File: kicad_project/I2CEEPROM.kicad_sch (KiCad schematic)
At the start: 3 parts, among them U15 24FC64-I/SN

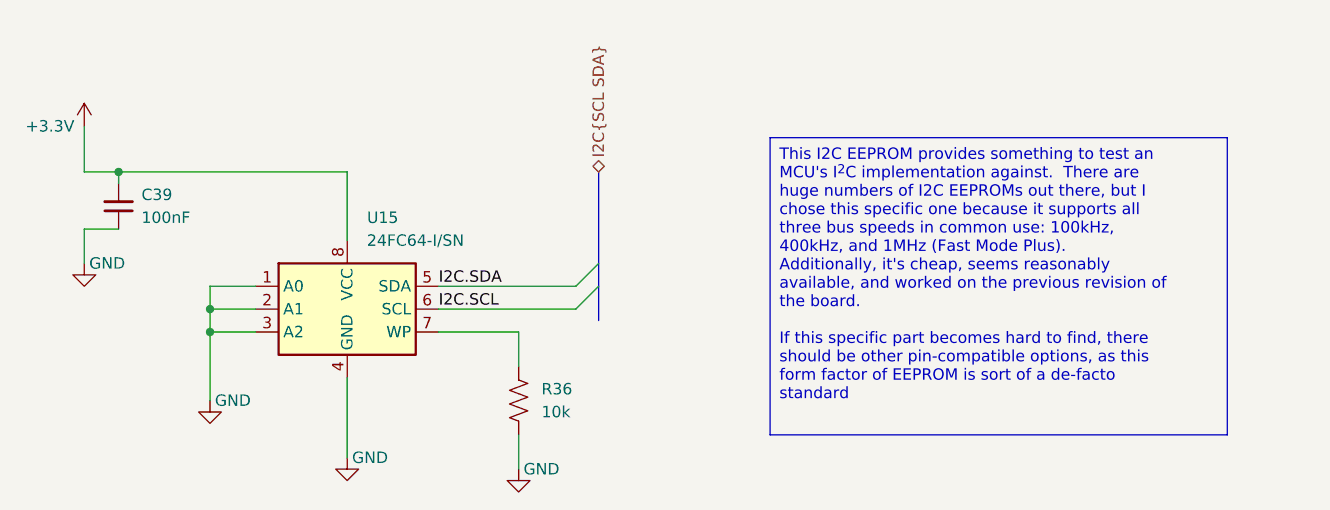
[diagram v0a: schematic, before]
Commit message: Switch out multiplexer, start switch FX2LP out for RP2040
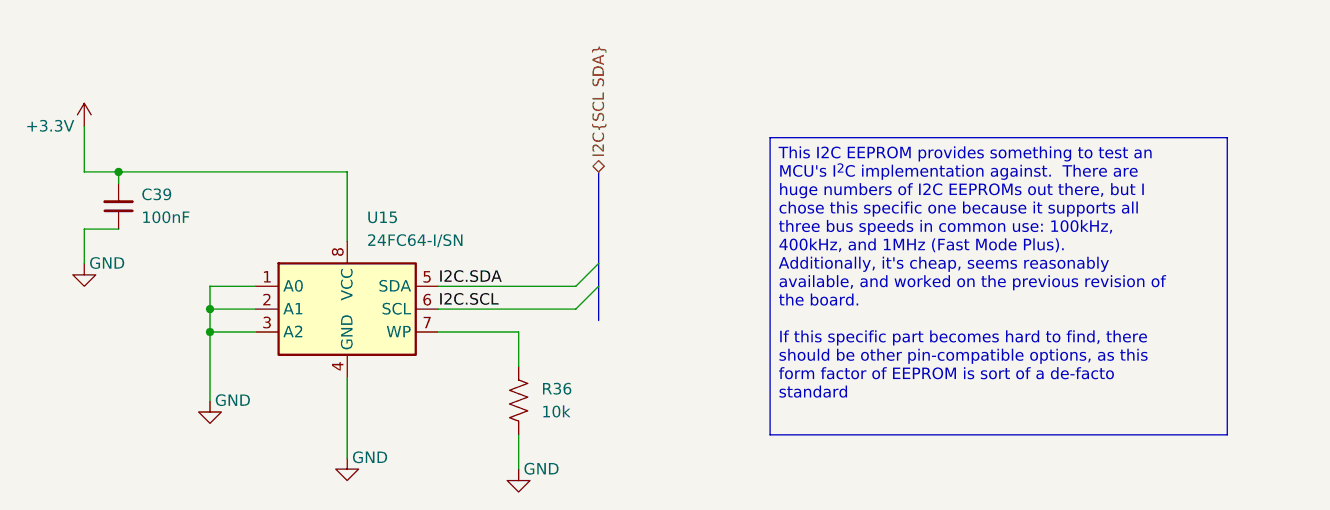
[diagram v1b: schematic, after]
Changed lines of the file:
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@@
 (kicad_sch
-	(version 20231120)
+	(version 20250114)
 	(generator "eeschema")
-	(generator_version "8.0")
+	(generator_version "9.0")
 	(paper "A5")
 	(title_block
@@
 		(comment 1 "EEPROM for the board to talk to over I^{2}C")
 	)
-	(junction
-		(at 67.31 53.34)
-		(diameter 0)
-		(color 0 0 0 0)
-	)
-	(junction
-		(at 77.47 68.58)
-		(diameter 0)
-		(color 0 0 0 0)
-	)
-	(junction
-		(at 77.47 71.12)
-		(diameter 0)
-		(color 0 0 0 0)
-	)
-	(bus_entry
-		(at 120.65 63.5)
-		(size -2.54 2.54)
-		(stroke
-			(width 0)
-			(type default)
-		)
-	)
-	(bus_entry
-		(at 120.65 66.04)
-		(size -2.54 2.54)
-		(stroke
-			(width 0)
-			(type default)
-		)
-	)
-	(wire
-		(pts
-			(xy 77.47 71.12) (xy 77.47 78.74)
-		)
-		(stroke
-			(width 0)
-			(type default)
-		)
-	)
-	(wire
-		(pts
-			(xy 77.47 68.58) (xy 77.47 71.12)
-		)
-		(stroke
-			(width 0)
-			(type default)
-		)
-	)
-	(wire
-		(pts
-			(xy 63.5 53.34) (xy 67.31 53.34)
-		)
-		(stroke
-			(width 0)
-			(type default)
-		)
-	)
-	(wire
-		(pts
-			(xy 67.31 53.34) (xy 67.31 54.61)
-		)
-		(stroke
-			(width 0)
-			(type default)
-		)
-	)
-	(wire
-		(pts
-			(xy 67.31 53.34) (xy 92.71 53.34)
-		)
-		(stroke
-			(width 0)
-			(type default)
-		)
-	)
-	(bus
-		(pts
-			(xy 120.65 53.34) (xy 120.65 63.5)
-		)
-		(stroke
-			(width 0)
-			(type default)
-		)
-	)
-	(wire
-		(pts
-			(xy 92.71 76.2) (xy 92.71 85.09)
-		)
-		(stroke
-			(width 0)
-			(type default)
-		)
-	)
-	(wire
-		(pts
-			(xy 82.55 68.58) (xy 77.47 68.58)
-		)
-		(stroke
-			(width 0)
-			(type default)
-		)
-	)
-	(wire
-		(pts
-			(xy 111.76 71.12) (xy 111.76 74.93)
-		)
-		(stroke
-			(width 0)
-			(type default)
-		)
-	)
-	(bus
-		(pts
-			(xy 120.65 63.5) (xy 120.65 66.04)
-		)
-		(stroke
-			(width 0)
-			(type default)
-		)
-	)
-	(wire
-		(pts
-			(xy 77.47 66.04) (xy 77.47 68.58)
-		)
-		(stroke
-			(width 0)
-			(type default)
-		)
-	)
-	(wire
-		(pts
-			(xy 67.31 59.69) (xy 63.5 59.69)
-		)
-		(stroke
-			(width 0)
-			(type default)
-		)
-	)
-	(wire
-		(pts
-			(xy 111.76 82.55) (xy 111.76 86.36)
-		)
-		(stroke
-			(width 0)
-			(type default)
-		)
-	)
-	(wire
-		(pts
-			(xy 63.5 59.69) (xy 63.5 63.5)
-		)
-		(stroke
-			(width 0)
-			(type default)
-		)
-	)
-	(wire
-		(pts
-			(xy 63.5 48.26) (xy 63.5 53.34)
-		)
-		(stroke
-			(width 0)
-			(type default)
-		)
-	)
-	(wire
-		(pts
-			(xy 102.87 71.12) (xy 111.76 71.12)
-		)
-		(stroke
-			(width 0)
-			(type default)
-		)
-	)
-	(wire
-		(pts
-			(xy 92.71 53.34) (xy 92.71 60.96)
-		)
-		(stroke
-			(width 0)
-			(type default)
-		)
-	)
-	(wire
-		(pts
-			(xy 82.55 66.04) (xy 77.47 66.04)
-		)
-		(stroke
-			(width 0)
-			(type default)
-		)
-	)
-	(wire
-		(pts
-			(xy 102.87 66.04) (xy 118.11 66.04)
-		)
-		(stroke
-			(width 0)
-			(type default)
-		)
-	)
-	(wire
-		(pts
-			(xy 82.55 71.12) (xy 77.47 71.12)
-		)
-		(stroke
-			(width 0)
-			(type default)
-		)
-	)
-	(wire
-		(pts
-			(xy 102.87 68.58) (xy 118.11 68.58)
-		)
-		(stroke
-			(width 0)
-			(type default)
-		)
-	)
-	(bus
-		(pts
-			(xy 120.65 66.04) (xy 120.65 69.85)
-		)
-		(stroke
-			(width 0)
-			(type default)
-		)
-	)
 	(text_box "This I2C EEPROM provides something to test an MCU's I^{2}C implementation against.  There are huge numbers of I2C EEPROMs out there, but I chose this specific one because it supports all three bus speeds in common use: 100kHz, 400kHz, and 1MHz (Fast Mode Plus).  Additionally, it's cheap, seems reasonably available, and worked on the previous revision of the board.\n\nIf this specific part becomes hard to find, there should be other pin-compatible options, as this form factor of EEPROM is sort of a de-facto standard"
 		(exclude_from_sim no)
 		(at 139.7 49.53 0)
 		(size 50.8 33.02)
+		(margins 0.9525 0.9525 0.9525 0.9525)
 		(stroke
 			(width 0)
@@
 		)
 	)
+	(junction
+		(at 67.31 53.34)
+		(diameter 0)
+		(color 0 0 0 0)
+	)
+	(junction
+		(at 77.47 68.58)
+		(diameter 0)
+		(color 0 0 0 0)
+	)
+	(junction
+		(at 77.47 71.12)
+		(diameter 0)
+		(color 0 0 0 0)
+	)
+	(bus_entry
+		(at 120.65 63.5)
+		(size -2.54 2.54)
+		(stroke
+			(width 0)
+			(type default)
+		)
+	)
+	(bus_entry
+		(at 120.65 66.04)
+		(size -2.54 2.54)
+		(stroke
+			(width 0)
+			(type default)
+		)
+	)
+	(wire
+		(pts
+			(xy 77.47 71.12) (xy 77.47 78.74)
+		)
+		(stroke
+			(width 0)
+			(type default)
+		)
+	)
+	(wire
+		(pts
+			(xy 77.47 68.58) (xy 77.47 71.12)
+		)
+		(stroke
+			(width 0)
+			(type default)
+		)
+	)
+	(wire
+		(pts
+			(xy 63.5 53.34) (xy 67.31 53.34)
+		)
+		(stroke
+			(width 0)
+			(type default)
+		)
+	)
+	(wire
+		(pts
+			(xy 67.31 53.34) (xy 67.31 54.61)
+		)
+		(stroke
+			(width 0)
+			(type default)
+		)
+	)
+	(wire
+		(pts
+			(xy 67.31 53.34) (xy 92.71 53.34)
+		)
+		(stroke
+			(width 0)
+			(type default)
+		)
+	)
+	(bus
+		(pts
+			(xy 120.65 53.34) (xy 120.65 63.5)
+		)
+		(stroke
+			(width 0)
+			(type default)
+		)
+	)
+	(wire
+		(pts
+			(xy 92.71 76.2) (xy 92.71 85.09)
+		)
+		(stroke
+			(width 0)
+			(type default)
+		)
+	)
+	(wire
+		(pts
+			(xy 82.55 68.58) (xy 77.47 68.58)
+		)
+		(stroke
+			(width 0)
+			(type default)
+		)
+	)
+	(wire
+		(pts
+			(xy 111.76 71.12) (xy 111.76 74.93)
+		)
+		(stroke
+			(width 0)
+			(type default)
+		)
+	)
+	(bus
+		(pts
+			(xy 120.65 63.5) (xy 120.65 66.04)
+		)
+		(stroke
+			(width 0)
+			(type default)
+		)
+	)
+	(wire
+		(pts
+			(xy 77.47 66.04) (xy 77.47 68.58)
+		)
+		(stroke
+			(width 0)
+			(type default)
+		)
+	)
+	(wire
+		(pts
+			(xy 67.31 59.69) (xy 63.5 59.69)
+		)
+		(stroke
+			(width 0)
+			(type default)
+		)
+	)
+	(wire
+		(pts
+			(xy 111.76 82.55) (xy 111.76 86.36)
+		)
+		(stroke
+			(width 0)
+			(type default)
+		)
+	)
+	(wire
+		(pts
+			(xy 63.5 59.69) (xy 63.5 63.5)
+		)
+		(stroke
+			(width 0)
+			(type default)
+		)
+	)
+	(wire
+		(pts
+			(xy 63.5 48.26) (xy 63.5 53.34)
+		)
+		(stroke
+			(width 0)
+			(type default)
+		)
+	)
+	(wire
+		(pts
+			(xy 102.87 71.12) (xy 111.76 71.12)
+		)
+		(stroke
+			(width 0)
+			(type default)
+		)
+	)
+	(wire
+		(pts
+			(xy 92.71 53.34) (xy 92.71 60.96)
+		)
+		(stroke
+			(width 0)
+			(type default)
+		)
+	)
+	(wire
+		(pts
+			(xy 82.55 66.04) (xy 77.47 66.04)
+		)
+		(stroke
+			(width 0)
+			(type default)
+		)
+	)
+	(wire
+		(pts
+			(xy 102.87 66.04) (xy 118.11 66.04)
+		)
+		(stroke
+			(width 0)
+			(type default)
+		)
+	)
+	(wire
+		(pts
+			(xy 82.55 71.12) (xy 77.47 71.12)
+		)
+		(stroke
+			(width 0)
+			(type default)
+		)
+	)
+	(wire
+		(pts
+			(xy 102.87 68.58) (xy 118.11 68.58)
+		)
+		(stroke
+			(width 0)
+			(type default)
+		)
+	)
+	(bus
+		(pts
+			(xy 120.65 66.04) (xy 120.65 69.85)
+		)
+		(stroke
+			(width 0)
+			(type default)
+		)
+	)
